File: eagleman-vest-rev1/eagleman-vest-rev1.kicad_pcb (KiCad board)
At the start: 2 copper layers, 50.5 x 81.7 mm, 102 parts, among them J1 Conn_01x08_Pin, J10 Screw_Terminal_01x02, J11 Screw_Terminal_01x02, J14 Conn_01x02_Pin, J15 Conn_01x06_Pin, J16 Conn_01x01_Pin, J17 Conn_01x08_Pin, J18 Conn_01x04_Pin, J19 Conn_01x06_Pin, J2 Screw_Terminal_01x02, J3 Screw_Terminal_01x02, J4 Screw_Terminal_01x02, J5 Screw_Terminal_01x02, J6 Screw_Terminal_01x02, J7 Screw_Terminal_01x02, J8 Screw_Terminal_01x02, J9 Screw_Terminal_01x02, P1 USB_C_Plug_USB2.0, SW1 SW_SPST, SW2 SW_SPST, U10 DRV2605LDGSR, U11 DRV2605LDGSR, U12 DRV2605LDGSR, U13 DRV2605LDGSR, U14 DRV2605LDGSR, U15 DRV2605LDGSR, U16 DRV2605LDGSR, U2 AP1117-33, U3 TCA9548APWR, U4 TCA9548APWR, U5 ESP32-S3-WROOM-1, U7 DRV2605LDGSR, U8 DRV2605LDGSR, U9 DRV2605LDGSR

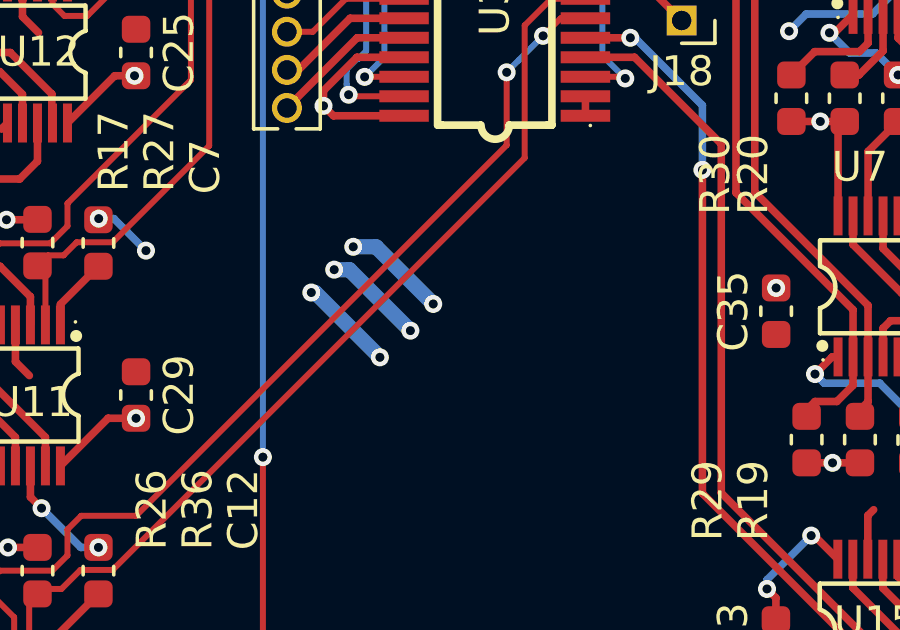
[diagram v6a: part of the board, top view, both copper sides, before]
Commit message: added manufacturing files
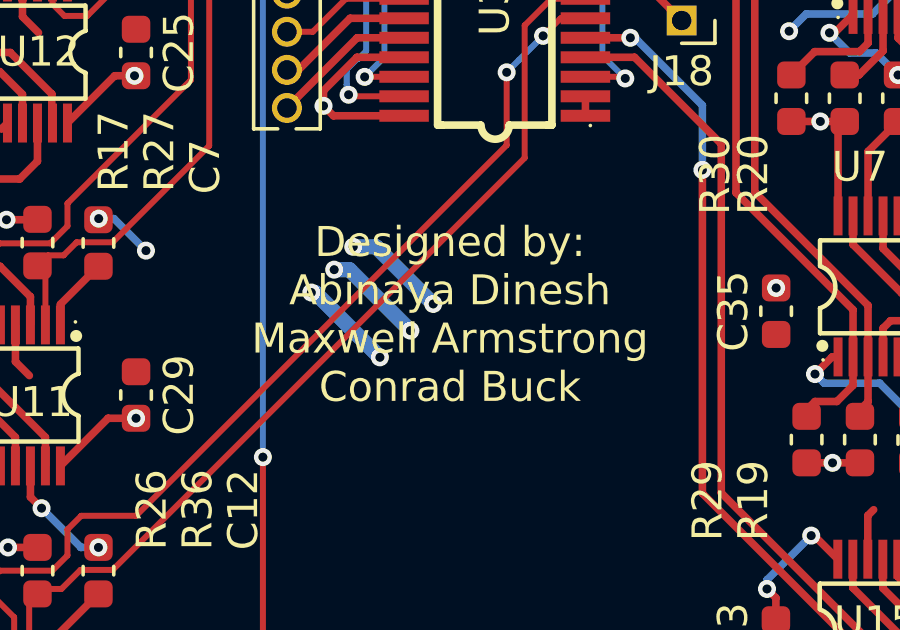
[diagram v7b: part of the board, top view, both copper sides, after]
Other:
- board text added: "Designed by: Abinaya Dinesh Maxwell Armstrong Conrad Buck"
- board text added: "Neurotech at Berkeley Haptic Feedback Vest Project Control Board rev1"
